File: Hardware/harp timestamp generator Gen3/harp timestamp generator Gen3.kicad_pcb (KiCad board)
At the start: 4 copper layers, 124.5 x 80.4 mm, 153 parts, among them IC1 MCP73831, IC10 SN74LVC1G125DBVT, IC11 LP5951MFX-3.3/NOPB, IC12 SI8621BC, IC13 SI8621BC, IC14 SI8621BC, IC15 SI8621BC, IC16 SI8621BC, IC17 SI8621BC, IC18 SN74LVC1G125DBVT, IC19 SN74LVC1G125DBVT, IC2 USBLC6-2SC6, IC3 FT232RL-REEL, IC4 TPS2114, IC5 LP5951MFX-3.3/NOPB, IC6 ATXMEGA16A4U-A, IC7 M74VHC1GT126DF1G, IC8 M74VHC1GT126DF1G, IC9 M74VHC1GT126DF1G, Q1 RTU002P02T106, Q2 BC817-40W, Q3 SBC817, Q4 DMG1012UW, Q5 DMP2035U-7, T1 BC850, T10 BC850, T2 BC850, T3 BC850, T4 BC850, T5 BC850, T6 BC850, T7 BC850, T8 BC850, T9 BC850, X1 B2B-XH-A(LF)(SN)

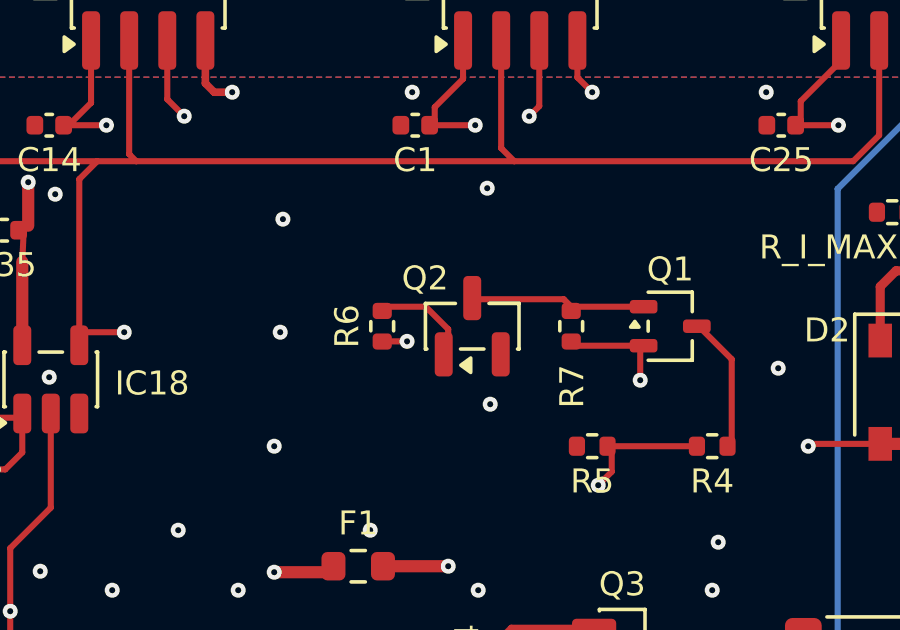
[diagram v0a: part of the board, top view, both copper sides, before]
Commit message: review após 1ª produção de placas teste
> harp timestamp generator Gen3
  . mudança da case de Q2
  . mudança de ligação em 'Button0'

> harp timestamp generator Gen3 front panel
  . acerto no recorte da ficha IDC e interruptor bateria
  . modificação de setup no logo 'harp'

> harp timestamp generator Gen3 rear panel
  . acerto no recorte de ficha USB
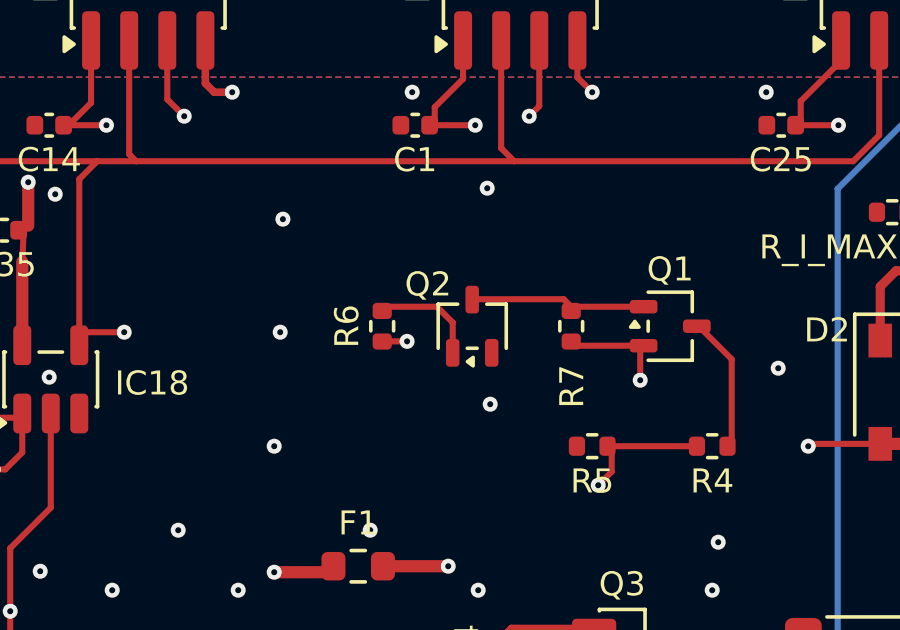
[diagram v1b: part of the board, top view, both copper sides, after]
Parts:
- Q2: footprint Package_TO_SOT_SMD:SOT-23 -> Package_TO_SOT_SMD:SOT-323_SC-70
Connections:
- BUTTON0 pad 1: unconnected-(BUTTON0-A-Pad1) -> GND
- BUTTON0 pad 3: GND -> unconnected-(BUTTON0-C-Pad3)
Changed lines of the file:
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@@
 			(size 1.7 0.7)
 			(layers "F.Cu" "F.Mask" "F.Paste")
-			(net "unconnected-(BUTTON0-A-Pad1)")
+			(net "GND")
 			(pinfunction "A_1")
-			(pintype "passive+no_connect")
+			(pintype "passive")
 			(solder_mask_margin 0)
 			(solder_paste_margin 0)
@@
 			(size 1.7 0.7)
 			(layers "F.Cu" "F.Mask" "F.Paste")
-			(net "GND")
+			(net "unconnected-(BUTTON0-C-Pad3)")
 			(pinfunction "C_3")
-			(pintype "passive")
+			(pintype "passive+no_connect")
 			(solder_mask_margin 0)
 			(solder_paste_margin 0)
@@
 		(embedded_fonts no)
 	)
-	(footprint "Package_TO_SOT_SMD:SOT-23"
+	(footprint "Package_TO_SOT_SMD:SOT-323_SC-70"
 		(layer "F.Cu")
 		(at 147.2711 98.1951 90)
-		(descr "SOT, 3 Pin (JEDEC TO-236 Var AB https://www.jedec.org/document_search?search_api_views_fulltext=TO-236)")
-		(tags "SOT TO_SOT_SMD")
+		(descr "SOT, 3 Pin (https://home.jeita.or.jp/tsc/std-pdf/ED-7500A.pdf#page=148)")
+		(tags "SOT TO_SOT_SMD SC-70 SOT-323")
 		(property "Reference" "Q2"
-			(at 1.5951 -1.5711 180)
+			(at 1.3951 -1.4711 0)
 			(layer "F.SilkS")
 			(effects
@@
 		)
 		(property "Value" "BC817-40W"
-			(at 0 2.4 90)
+			(at 0 1.8 90)
 			(layer "F.Fab")
 			(effects
@@
 		(duplicate_pad_numbers_are_jumpers no)
 		(fp_line
-			(start 0.76 -1.56)
-			(end 0.76 -0.56)
-			(stroke
-				(width 0.12)
-				(type solid)
-			)
-			(layer "F.SilkS")
-		)
-		(fp_line
-			(start -0.76 -1.56)
-			(end 0.76 -1.56)
-			(stroke
-				(width 0.12)
-				(type solid)
-			)
-			(layer "F.SilkS")
-		)
-		(fp_line
-			(start -0.76 -1.51)
-			(end -0.76 -1.56)
+			(start 0.735 -1.135)
+			(end 0.735 -0.485)
 			(stroke
 				(width 0.12)
@@
 		)
 		(fp_line
-			(start -0.76 0.39)
-			(end -0.76 -0.39)
+			(start -0.735 -1.135)
+			(end 0.735 -1.135)
 			(stroke
 				(width 0.12)
@@
 		)
 		(fp_line
-			(start 0.76 0.56)
-			(end 0.76 1.56)
+			(start -0.735 0.165)
+			(end -0.735 -0.165)
 			(stroke
 				(width 0.12)
@@
 		)
 		(fp_line
-			(start 0.76 1.56)
-			(end -0.76 1.56)
+			(start 0.735 0.485)
+			(end 0.735 1.135)
 			(stroke
 				(width 0.12)
@@
 		)
 		(fp_line
-			(start -0.76 1.56)
-			(end -0.76 1.51)
+			(start 0.735 1.135)
+			(end -0.735 1.135)
 			(stroke
 				(width 0.12)
@@
 		(fp_poly
 			(pts
-				(xy -1.3 -0.38) (xy -1.06 -0.05) (xy -1.54 -0.05)
+				(xy -1.18 -0.16) (xy -1.04 0.03) (xy -1.32 0.03)
 			)
 			(stroke
@@
 		)
 		(fp_line
-			(start 0.9 -1.7)
-			(end 0.9 -0.55)
+			(start 0.73 -1.1)
+			(end 0.73 -0.33)
 			(stroke
 				(width 0.05)
@@
 		)
 		(fp_line
-			(start -0.9 -1.7)
-			(end 0.9 -1.7)
+			(start -0.73 -1.1)
+			(end 0.73 -1.1)
 			(stroke
 				(width 0.05)
@@
 		)
 		(fp_line
-			(start -0.9 -1.5)
-			(end -0.9 -1.7)
+			(start -0.73 -0.98)
+			(end -0.73 -1.1)
 			(stroke
 				(width 0.05)
@@
 		)
 		(fp_line
-			(start -1.93 -1.5)
-			(end -0.9 -1.5)
+			(start -1.45 -0.98)
+			(end -0.73 -0.98)
 			(stroke
 				(width 0.05)
@@
 		)
 		(fp_line
-			(start 1.93 -0.55)
-			(end 1.93 0.55)
+			(start 1.45 -0.33)
+			(end 1.45 0.33)
 			(stroke
 				(width 0.05)
@@
 		)
 		(fp_line
-			(start 0.9 -0.55)
-			(end 1.93 -0.55)
+			(start 0.73 -0.33)
+			(end 1.45 -0.33)
 			(stroke
 				(width 0.05)
@@
 		)
 		(fp_line
-			(start -0.9 -0.39)
-			(end -1.93 -0.39)
+			(start -0.73 -0.32)
+			(end -1.45 -0.32)
 			(stroke
 				(width 0.05)
@@
 		)
 		(fp_line
-			(start -1.93 -0.39)
-			(end -1.93 -1.5)
+			(start -1.45 -0.32)
+			(end -1.45 -0.98)
 			(stroke
 				(width 0.05)
@@
 		)
 		(fp_line
-			(start -0.9 0.39)
-			(end -0.9 -0.39)
+			(start -0.73 0.32)
+			(end -0.73 -0.32)
 			(stroke
 				(width 0.05)
@@
 		)
 		(fp_line
-			(start -1.93 0.39)
-			(end -0.9 0.39)
+			(start -1.45 0.32)
+			(end -0.73 0.32)
 			(stroke
 				(width 0.05)
@@
 		)
 		(fp_line
-			(start 1.93 0.55)
-			(end 0.9 0.55)
+			(start 1.45 0.33)
+			(end 0.73 0.33)
 			(stroke
 				(width 0.05)
@@
 		)
 		(fp_line
-			(start 0.9 0.55)
-			(end 0.9 1.7)
+			(start 0.73 0.33)
+			(end 0.73 1.1)
 			(stroke
 				(width 0.05)
@@
 		)
 		(fp_line
-			(start -0.9 1.5)
-			(end -1.93 1.5)
+			(start -0.73 0.98)
+			(end -1.45 0.98)
 			(stroke
 				(width 0.05)
@@
 		)
 		(fp_line
-			(start -1.93 1.5)
-			(end -1.93 0.39)
+			(start -1.45 0.98)
+			(end -1.45 0.32)
 			(stroke
 				(width 0.05)
@@
 		)
 		(fp_line
-			(start 0.9 1.7)
-			(end -0.9 1.7)
+			(start 0.73 1.1)
+			(end -0.73 1.1)
 			(stroke
 				(width 0.05)
@@
 		)
 		(fp_line
-			(start -0.9 1.7)
-			(end -0.9 1.5)
+			(start -0.73 1.1)
+			(end -0.73 0.98)
 			(stroke
 				(width 0.05)
@@
 		(fp_poly
 			(pts
-				(xy -0.325 -1.45) (xy 0.65 -1.45) (xy 0.65 1.45) (xy -0.65 1.45) (xy -0.65 -1.125)
+				(xy -0.3125 -1) (xy 0.625 -1) (xy 0.625 1) (xy -0.625 1) (xy -0.625 -0.6875)
 			)
 			(stroke
@@
 			(effects
 				(font
-					(size 0.72 0.72)
-					(thickness 0.11)
+					(size 0.5 0.5)
+					(thickness 0.08)
 				)
 			)
 		)
 		(pad "1" smd roundrect
-			(at -0.9375 -0.95 90)
-			(size 1.475 0.6)
+			(at -0.8875 -0.65 90)
+			(size 0.925 0.45)
 			(layers "F.Cu" "F.Mask" "F.Paste")
 			(roundrect_rratio 0.25)
@@
 		)
 		(pad "2" smd roundrect
-			(at -0.9375 0.95 90)
-			(size 1.475 0.6)
+			(at -0.8875 0.65 90)
+			(size 0.925 0.45)
 			(layers "F.Cu" "F.Mask" "F.Paste")
 			(roundrect_rratio 0.25)
@@
 		)
 		(pad "3" smd roundrect
-			(at 0.9375 0 90)
-			(size 1.475 0.6)
+			(at 0.8875 0 90)
+			(size 0.925 0.45)
 			(layers "F.Cu" "F.Mask" "F.Paste")
 			(roundrect_rratio 0.25)
@@
 		)
 		(embedded_fonts no)
-		(model "${KICAD10_3DMODEL_DIR}/Package_TO_SOT_SMD.3dshapes/SOT-23.step"
+		(model "${KICAD10_3DMODEL_DIR}/Package_TO_SOT_SMD.3dshapes/SOT-323_SC-70.step"
 			(offset
 				(xyz 0 0 0)
@@
 	)
 	(segment
-		(start 144.2711 97.5451)
-		(end 145.7211 97.5451)
+		(start 146.0951 97.5451)
+		(end 146.6211 98.0711)
 		(width 0.2032)
 		(layer "F.Cu")
@@
 	)
 	(segment
-		(start 146.4711 98.2951)
-		(end 146.4711 98.9451)
+		(start 144.2711 97.5451)
+		(end 146.0951 97.5451)
 		(width 0.2032)
 		(layer "F.Cu")
@@
 	)
 	(segment
-		(start 145.7211 97.5451)
-		(end 146.4711 98.2951)
+		(start 146.6211 98.0711)
+		(end 146.6211 99.0826)
 		(width 0.2032)
 		(layer "F.Cu")
